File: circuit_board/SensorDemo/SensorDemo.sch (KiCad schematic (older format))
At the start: 14 parts, among them J1 BARREL_JACK, SW1 SWITCH_SPDT, U1 TLV1117-33CDCYR, U2 MCP4821, U3 dsPIC33EP32GP502

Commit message: updated schematic & footprints
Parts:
- added D2, D3: LED, SensorDemo_pcb:LED0805, symbol SensorDemo_passive:LED
- added J2: USB2_MICRO, symbol SensorDemo_connector:USB2_MICRO
- added PS01, PS04, PS06, PS08: GND, symbol SensorDemo_power_supply:GND
- added PS03, PS05, PS07, PS?: +3V3, symbol SensorDemo_power_supply:+3V3
- added R2, R3: R, SensorDemo_pcb:R0805, symbol SensorDemo_passive:R
- added RV1, RV2: POT, symbol SensorDemo_passive:POT
- added U4: FT232RL, SensorDemo_pcb:DIP_28_300, symbol SensorDemo_IC:FT232RL
- added U5: INA126, SensorDemo_pcb:DIP_8_300, symbol SensorDemo_IC:INA126
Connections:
- net labels added: USBDM, USBDP, VCCIO, sensVal, ucCTS, ucRTS, ucTX
- wire segments 68 -> 115
- no-connect marks 3 -> 2

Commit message: schematic comments made
minor updates:
edited schematic library to make some parts look better
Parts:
- removed PS01, PS04, PS06, PS08: GND, symbol SensorDemo_power_supply:GND
- removed PS03, PS05, PS07, PS?: +3V3, symbol SensorDemo_power_supply:+3V3
- R1: value 330R -> 1k
- R2, R3: value R -> 1k
- renumbered U3 to U2, U2 to U3, U5 to U4, U4 to U5
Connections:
- wire segments 115 -> 122
- no-connect marks 2 -> 3
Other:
- note added: "VCC from a standard USB port is 5V,\nwe should filter it and feed it into a LDO.\nplease check the video I shared and edit\naccordingly."
- note added: "check INA126 datasheet fig.25\nfor example circuit. check the REF1004"
- note added: "connect power"
- note added: "include a RX line also"
- note added: "let's remove the power switch and the barrel jack,\ninstead, we should use the power line from the USB\nto supply the raw 5V power to the 3.3V LDO."
- note added: "missing Vcap"
- note added: "two things we can do:\n1. change the INA to something with\nprogrammable gain\n2. find a surface mount pot."
- note added: "use wires to connect components.\nuse 90 degree angle on wire when cornering.\nthis would increase clarity.\nplease modify others accordingly\n\nuncheck the "footprint" and the\n"datasheet" property from components.\ndelete after read.\n"
- moved on the sheet: C1, C2, C3, C4, C5, C6, C7, D1, D2, D3, R1, R2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

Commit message: schematic changes
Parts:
- removed C1: 10uF, SensorDemo_pcb:C0805, symbol SensorDemo_passive:C
- removed C2, C3, C6: 1uF, SensorDemo_pcb:C0805, symbol SensorDemo_passive:C
- removed C4, C5, C7: 100nF, SensorDemo_pcb:C0805, symbol SensorDemo_passive:C
- removed J1: BARREL_JACK, Global PCB Library:BARREL_JACK, symbol SensorDemo_connector:BARREL_JACK
- removed RV2: POT, symbol SensorDemo_passive:POT
- removed SW1: SWITCH_SPDT, SensorDemo_pcb:SW_OS102011MA1QN1, symbol SensorDemo_discrete:SWITCH_SPDT
- removed U3: MCP4821, SensorDemo_pcb:SOIC-8, symbol SensorDemo_IC:MCP4821
- added C?: 10nF, symbol SensorDemo_passive:C
- added C? (x3): 1uF, symbol SensorDemo_passive:C
- added C? (x3): 100nF, symbol SensorDemo_passive:C
- added EC?: 10uF, symbol SensorDemo_passive:EC
- added FB?: FB, symbol SensorDemo_passive:FB
- added PS?: GND, symbol SensorDemo_power_supply:GND
- added U?: LTC1658, symbol SensorDemo_IC:LTC1658
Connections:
- net labels added: dacVout, ucRX
- wire segments 122 -> 118
- no-connect marks 3 -> 1
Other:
- note added: "12.3071 nano ohm"
- note removed: "connect power"
- note removed: "include a RX line also"
- note removed: "missing Vcap"
- note removed: "use wires to connect components.\nuse 90 degree angle on wire when cornering.\nthis would increase clarity.\nplease modify others accordingly\n\nuncheck the "footprint" and the\n"datasheet" property from components.\ndelete after read.\n"
- moved on the sheet: D1, J2, R1, U1

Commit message: add some comments
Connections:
- wire segments 118 -> 116
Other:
- note added: "Let's use a fixed resister here."
- note added: "copy other 3V3 symbols"
- note added: "create a reset circuit,\nyou can refer to the datasheet."
- note added: "do you have ucCTS on uC?\nsame as ucRTS.\nwhat about the TXD line?"
- note added: "use wires to connect them\nwhen close enough."
- note removed: "VCC from a standard USB port is 5V,\nwe should filter it and feed it into a LDO.\nplease check the video I shared and edit\naccordingly."
- note removed: "let's remove the power switch and the barrel jack,\ninstead, we should use the power line from the USB\nto supply the raw 5V power to the 3.3V LDO."
- note removed: "two things we can do:\n1. change the INA to something with\nprogrammable gain\n2. find a surface mount pot."
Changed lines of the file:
@@
-$EndComp
-$Comp
-L SensorDemo_power_supply:GND #PS08
-U 1 1 6026B9E7
-P 9100 4450
-F 0 "#PS08" H 9100 4325 50  0001 C CNN
-F 1 "GND" H 9100 4375 50  0001 C CNN
-F 2 "" H 9100 4450 50  0001 C CNN
-F 3 "" H 9100 4450 50  0001 C CNN
-	1    9100 4450
-	1    0    0    -1
 $EndComp
 $Comp
@@
 	5600 4750 5800 4750
 Connection ~ 5600 4750
-Text Notes 900  7150 0    50   ~ 0
-let's remove the power switch and the barrel jack,\ninstead, we should use the power line from the USB\nto supply the raw 5V power to the 3.3V LDO.
 NoConn ~ 2400 1300
-Text Notes 1850 -100 0    50   ~ 0
-VCC from a standard USB port is 5V,\nwe should filter it and feed it into a LDO.\nplease check the video I shared and edit\naccordingly.
 Wire Notes Line
 	6100 2300 6100 2800
@@
 	6750 2300 6100 2300
 Text Notes 6800 2650 0    50   ~ 0
-two things we can do:\n1. change the INA to something with\nprogrammable gain\n2. find a surface mount pot.
-Text Notes 7600 4800 0    50   ~ 0
-check INA126 datasheet fig.25\nfor example circuit. check the REF1004
+Let's use a fixed resister here.
 $Comp
 L SensorDemo_IC:LTC1658 U?
@@
 	2750 1500 2450 1500
 Connection ~ 6450 1000
-Wire Wire Line
-	6450 1000 6550 1000
 Connection ~ 6750 1000
 Wire Wire Line
-	6750 1000 7100 1000
+	6750 1000 6900 1000
 Wire Wire Line
 	2750 1500 3500 1500
@@
 Wire Wire Line
 	6750 1500 7600 1500
-Wire Wire Line
-	6550 850  6550 1000
-Connection ~ 6550 1000
-Wire Wire Line
-	6550 1000 6750 1000
-Text Label 6350 850  0    50   ~ 0
-+3V3
-Wire Wire Line
-	6350 850  6550 850
 Text Notes 2800 850  0    50   ~ 0
 12.3071 nano ohm
@@
 	1000 3650 1350 3650
 Wire Wire Line
-	2700 2300 2700 2450
-Wire Wire Line
 	2700 2450 2650 2450
 Wire Wire Line
 	2700 3250 2650 3250
-Connection ~ 2700 2450
-Wire Wire Line
-	2900 2300 2700 2300
-Text Label 2900 2300 2    50   ~ 0
-+3V3
 Wire Wire Line
 	2750 2550 2750 3350
@@
 Wire Wire Line
 	2750 3350 2750 4000
+$Comp
+L SensorDemo_power_supply:+3V3 #PS?
+U 1 1 6025A9BB
+P 6900 900
+F 0 "#PS?" H 6900 850 50  0001 C CNN
+F 1 "+3V3" H 6800 1000 50  0000 L CNN
+F 2 "" H 6905 595 50  0001 C CNN
+F 3 "" H 6905 595 50  0001 C CNN
+	1    6900 900
+	1    0    0    -1
+$EndComp
+Wire Wire Line
+	6450 1000 6750 1000
+Wire Wire Line
+	6900 900  6900 1000
+Connection ~ 6900 1000
+Wire Wire Line
+	6900 1000 7100 1000
+$Comp
+L SensorDemo_power_supply:+3V3 #PS?
+U 1 1 60267105
+P 2700 2250
+F 0 "#PS?" H 2700 2200 50  0001 C CNN
+F 1 "+3V3" H 2600 2350 50  0000 L CNN
+F 2 "" H 2705 1945 50  0001 C CNN
+F 3 "" H 2705 1945 50  0001 C CNN
+	1    2700 2250
+	1    0    0    -1
+$EndComp
+Wire Wire Line
+	2700 2250 2700 2450
+Connection ~ 2700 2450
+Wire Notes Line
+	1100 2300 1100 2500
+Wire Notes Line
+	1100 2500 1900 2500
+Wire Notes Line
+	1900 2500 1900 2300
+Wire Notes Line
+	1900 2300 1100 2300
+Text Notes 750  2150 0    50   ~ 0
+create a reset circuit,\nyou can refer to the datasheet.
+Text Notes 7600 4800 0    50   ~ 0
+check INA126 datasheet fig.25\nfor example circuit. check the REF1004
+Wire Notes Line
+	4250 4800 4250 5300
+Wire Notes Line
+	4250 5300 3350 5300
+Wire Notes Line
+	3350 5300 3350 4800
+Wire Notes Line
+	3350 4800 4250 4800
+Text Notes 3250 4750 0    50   ~ 0
+do you have ucCTS on uC?\nsame as ucRTS.\nwhat about the TXD line?
+Wire Notes Line
+	4850 4650 4850 4950
+Wire Notes Line
+	4850 4950 5200 4950
+Wire Notes Line
+	5200 4950 5200 4650
+Wire Notes Line
+	5200 4650 4850 4650
+Text Notes 4600 4650 0    50   ~ 0
+copy other 3V3 symbols
+Wire Notes Line
+	4150 3000 4150 3800
+Wire Notes Line
+	4150 3800 2850 3800
+Wire Notes Line
+	2850 3800 2850 3300
+Wire Notes Line
+	2850 3300 3650 3300
+Wire Notes Line
+	3650 3300 3650 3000
+Wire Notes Line
+	3650 3000 4150 3000
+Text Notes 3100 3700 0    50   ~ 0
+use wires to connect them\nwhen close enough.
 $EndSCHEMATC

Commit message: updated schematic
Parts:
- removed RV1: POT, symbol SensorDemo_passive:POT
- added C?: .01uF, symbol SensorDemo_passive:C
- added K?: PB, symbol SensorDemo_discrete:PB
- added PS? (x2): GND, symbol SensorDemo_power_supply:GND
- added PS? (x5): +3V3, symbol SensorDemo_power_supply:+3V3
- added R?: 10k, symbol SensorDemo_passive:R
- added R?: R, symbol SensorDemo_passive:R
- added U?: REF1933, symbol SensorDemo_IC:REF1933
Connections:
- net labels added: Vbias, Vref, ucEN
- net labels removed: ucCTS, ucRTS
- wire segments 116 -> 134
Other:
- note removed: "Let's use a fixed resister here."
- note removed: "check INA126 datasheet fig.25\nfor example circuit. check the REF1004"
- note removed: "copy other 3V3 symbols"
- note removed: "create a reset circuit,\nyou can refer to the datasheet."
- note removed: "do you have ucCTS on uC?\nsame as ucRTS.\nwhat about the TXD line?"
- note removed: "use wires to connect them\nwhen close enough."
- moved on the sheet: U2, U4, U?

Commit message: updated schematic
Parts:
- removed PS?: +3V3, symbol SensorDemo_power_supply:+3V3
- added C?: .1uF, symbol SensorDemo_passive:C
- added C? (x2): C, symbol SensorDemo_passive:C
- added PS?: +3V3, symbol SensorDemo_power_supply:+3V3
- U?: value REF1933 -> REF1930
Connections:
- wire segments 134 -> 153
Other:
- moved on the sheet: U2, U?

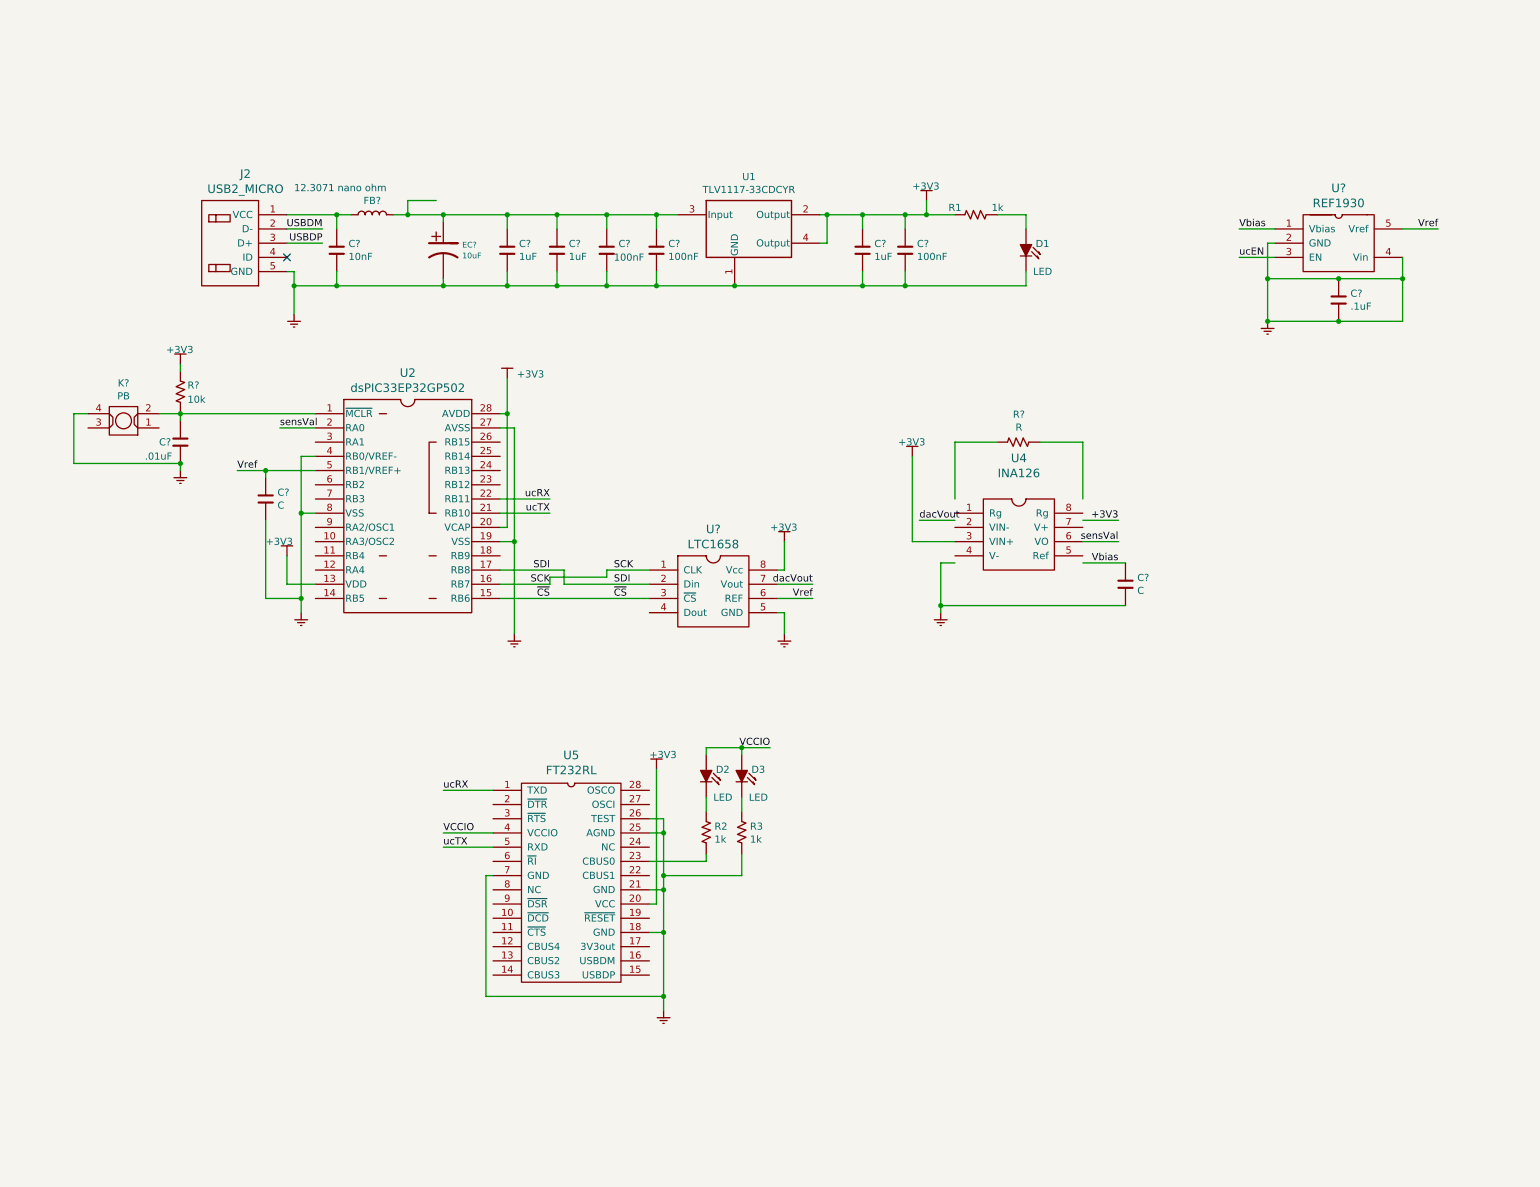
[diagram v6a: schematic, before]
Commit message: schematic edited
1. Let's use another REF1930 to bias the sensors. limit current to 15mA (20mA maximum) for safe operation.
2. FBC filter added to AVDD pin. value FB value needed.
3. sensor circuit included, with the position of two current limiting resistors.
4. bypass and decouple caps are added to INA & DAC power lines.
5. to Daniel: please add crystal circuit to the MCU, and finish the FT232 circuit.
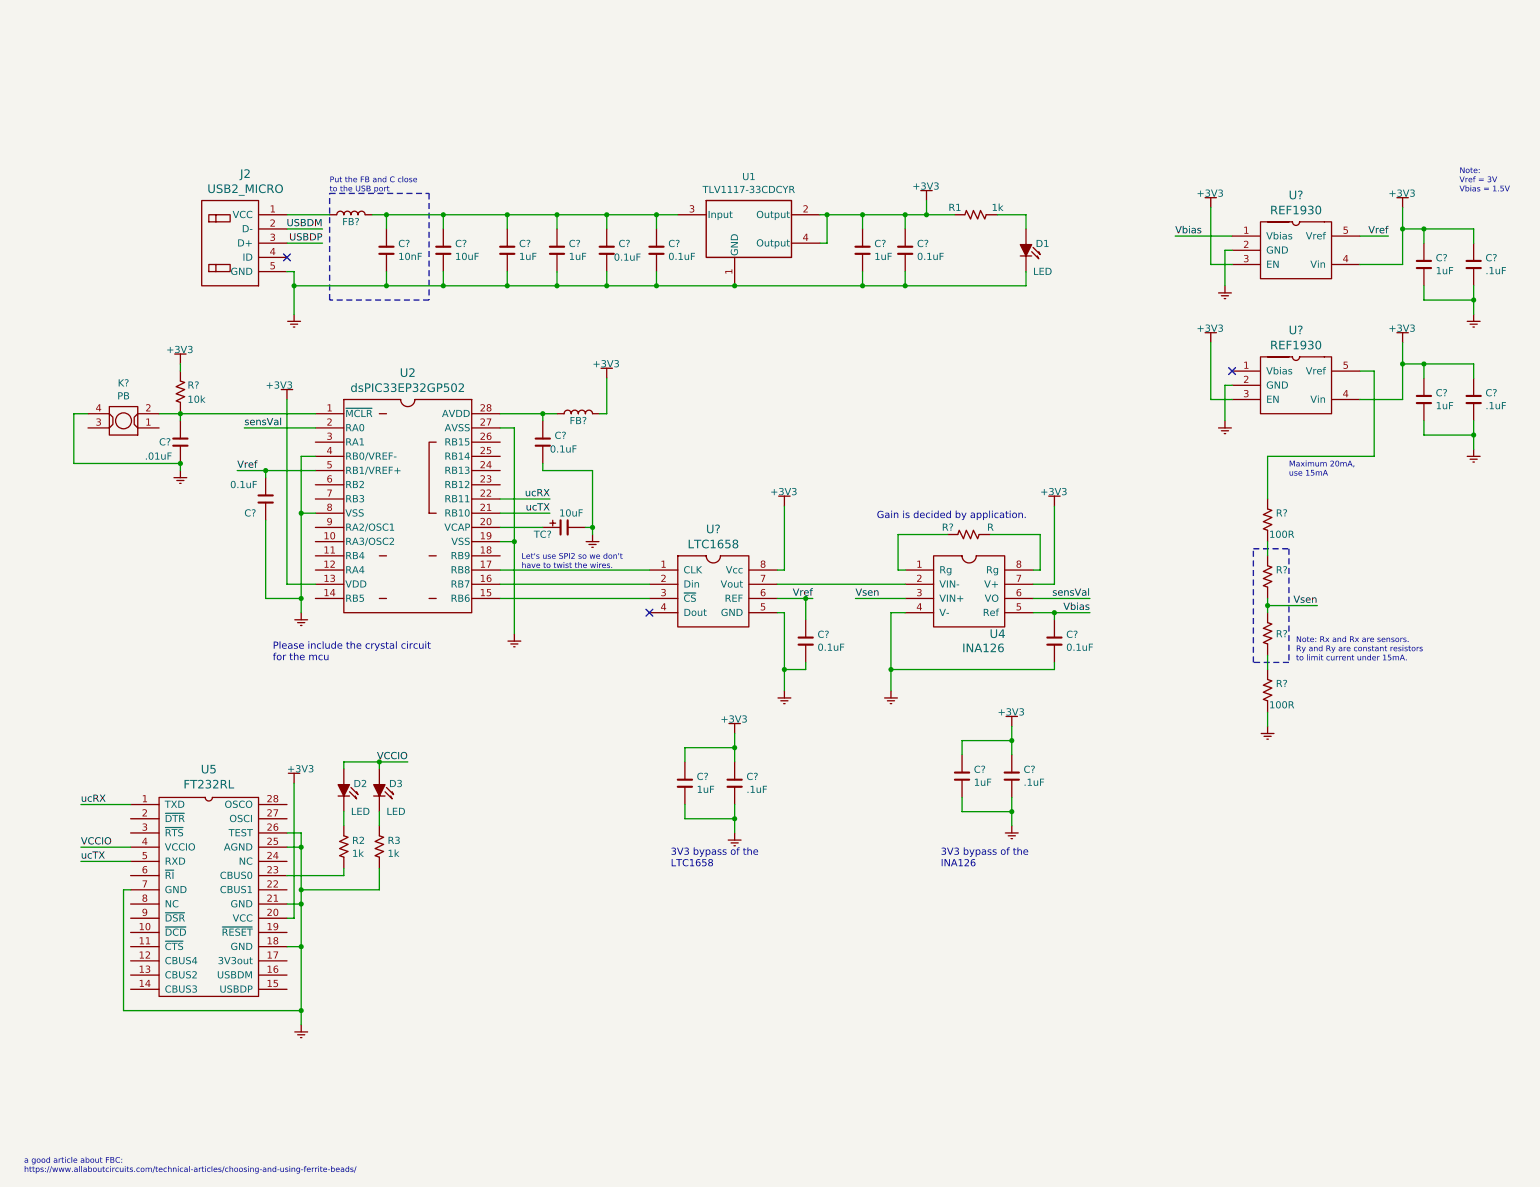
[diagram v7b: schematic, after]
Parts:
- removed EC?: 10uF, symbol SensorDemo_passive:EC
- added C? (x3): 1uF, symbol SensorDemo_passive:C
- added C? (x4): .1uF, symbol SensorDemo_passive:C
- added C? (x2): 0.1uF, symbol SensorDemo_passive:C
- added C?: 10uF, symbol SensorDemo_passive:C
- added FB?: 12.3071 nano ohm, symbol SensorDemo_passive:FB
- added PS? (x5): GND, symbol SensorDemo_power_supply:GND
- added PS? (x2): +3V3, symbol SensorDemo_power_supply:+3V3
- added R? (x2): 100R, symbol SensorDemo_passive:R
- added R? (x2): R, symbol SensorDemo_passive:R
- added TC?: 10uF, symbol SensorDemo_passive:TC
- added U?: REF1930, symbol SensorDemo_IC:REF1933
- C? (x3): value 100nF -> 0.1uF
- C?: value .1uF -> 1uF
- C? (x2): value C -> 0.1uF
- FB?: value FB -> 12.3071 nano ohm
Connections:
- net labels added: Vsen
- net labels removed: SCK, SDI, dacVout, ucEN, ~CS
- wire segments 153 -> 206
- no-connect marks 1 -> 3
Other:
- note added: "3V3 bypass of the \nINA126"
- note added: "3V3 bypass of the \nLTC1658"
- note added: "Gain is decided by application."
- note added: "Let's use SPI2 so we don't\nhave to twist the wires."
- note added: "Maximum 20mA,\nuse 15mA"
- note added: "Note: Rx and Rx are sensors.\nRy and Ry are constant resistors\nto limit current under 15mA."
- note added: "Note:\nVref = 3V\nVbias = 1.5V"
- note added: "Please include the crystal circuit\nfor the mcu"
- note added: "Put the FB and C close\nto the USB port"
- note added: "a good article about FBC:\nhttps://www.allaboutcircuits.com/technical-articles/choosing-and-using-ferrite-beads/"
- note removed: "12.3071 nano ohm"
- moved on the sheet: C?, D2, D3, FB?, R2, R3, R?, U4, U5, U?

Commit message: updated schematic
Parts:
- removed D2, D3: LED, SensorDemo_pcb:LED0805, symbol SensorDemo_passive:LED
- removed J2: USB2_MICRO, symbol SensorDemo_connector:USB2_MICRO
- removed PS?: +3V3, symbol SensorDemo_power_supply:+3V3
- removed R2, R3: 1k, SensorDemo_pcb:R0805, symbol SensorDemo_passive:R
- removed U5: FT232RL, SensorDemo_pcb:DIP_28_300, symbol SensorDemo_IC:FT232RL
- added C? (x2): C, symbol SensorDemo_passive:C
- added P?: CONN3X2, symbol SensorDemo_connector:CONN3X2
- added PS?: GND, symbol SensorDemo_power_supply:GND
- added R?: R, symbol SensorDemo_passive:R
- added R? (x2): 0, symbol SensorDemo_passive:R
- added X?: CRYSTAL, symbol SensorDemo_discrete:CRYSTAL
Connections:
- net PGC: now reaches U2.6 (RB2)
- net PGC: now also P?.5
- net PGD: now reaches U2.7 (RB3)
- net PGD: now also P?.4
- net at C?.2, C?.2, C?.2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: now also P?.3
- net Sensor: now reaches C?.1, C?.1, R1.1, U1.2 (Output), U1.4 (Output)
- net Sensor: now also R?.1
- net VDD: now reaches FB?.1
- net VDD: now also P?.2
- net at U?.5 (Vref): now also R?.2; no longer R?.1
- new net: C?.1, R?.1, X?.1
- new net: C?.1, R?.2, X?.2
- new net: C?.2, C?.2, PS?.1 (GND)
- new net: R?.1, R?.1, R?.2
- new net PGM: P?.6
- new net ~MCLR: P?.1
- no-connect marks 3 -> 2
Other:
- moved on the sheet: C?
